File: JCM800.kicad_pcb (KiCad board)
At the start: 2 copper layers, 258.5 x 77.3 mm, 113 parts, among them U1 ECC83, U2 ECC83, U3 ECC83, U4 EL84, U5 EL84

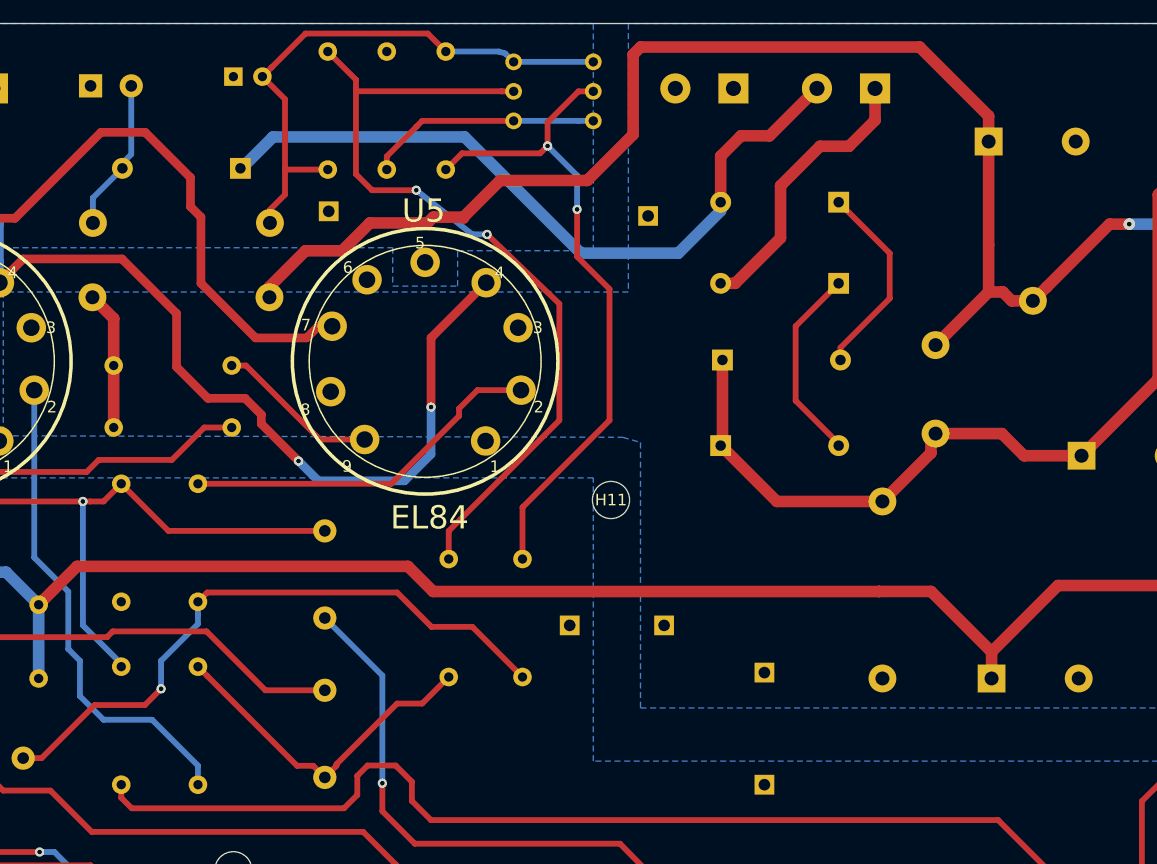
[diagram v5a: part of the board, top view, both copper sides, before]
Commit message: Fixed bias circuit
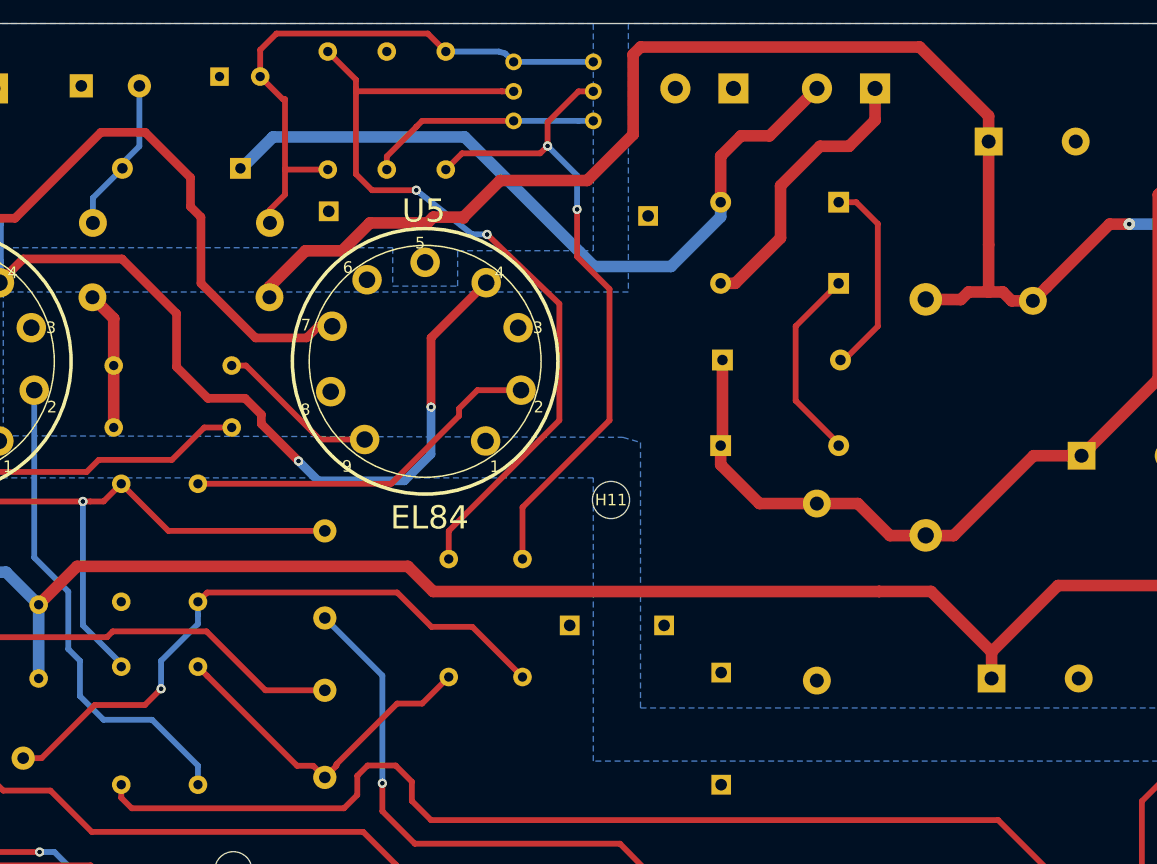
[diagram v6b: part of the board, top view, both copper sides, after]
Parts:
- C23: footprint Capacitor_THT:CP_Radial_D10.0mm_P3.50mm -> Capacitor_THT:CP_Radial_D10.0mm_P5.00mm
- C24: value 68uF/35V -> 100uF/35V; footprint Capacitor_THT:CP_Radial_D6.3mm_P2.50mm -> Capacitor_THT:CP_Radial_D8.0mm_P3.50mm
- R11: footprint Resistor_THT:R_Axial_DIN0922_L20.0mm_D9.0mm_P7.62mm_Vertical -> Resistor_THT:R_Axial_DIN0614_L14.3mm_D5.7mm_P20.32mm_Horizontal
- moved R8 5.65 mm to (240.2, 109.4)
- moved R11 4.03 mm to (249.6, 76.6)
- moved GND6 3.72 mm to (232.0, 108.7)
- moved GND7 3.72 mm to (232.0, 118.4)
- moved LOGO1 1.20 mm to (97.6, 108.9)
- moved C24 1.19 mm to (188.8, 57.4)
- moved C23 0.80 mm to (176.9, 58.2)
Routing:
- net /Tin2: track 63.6 -> 65.5 mm
- net Net-(BIAS_U4-Pad1): track 48.6 -> 50.3 mm
- net /A: track 75.4 -> 76.5 mm
- net /B: track 121.7 -> 120.9 mm
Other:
- rule pad_to_mask_clearance: 0.051 -> 0

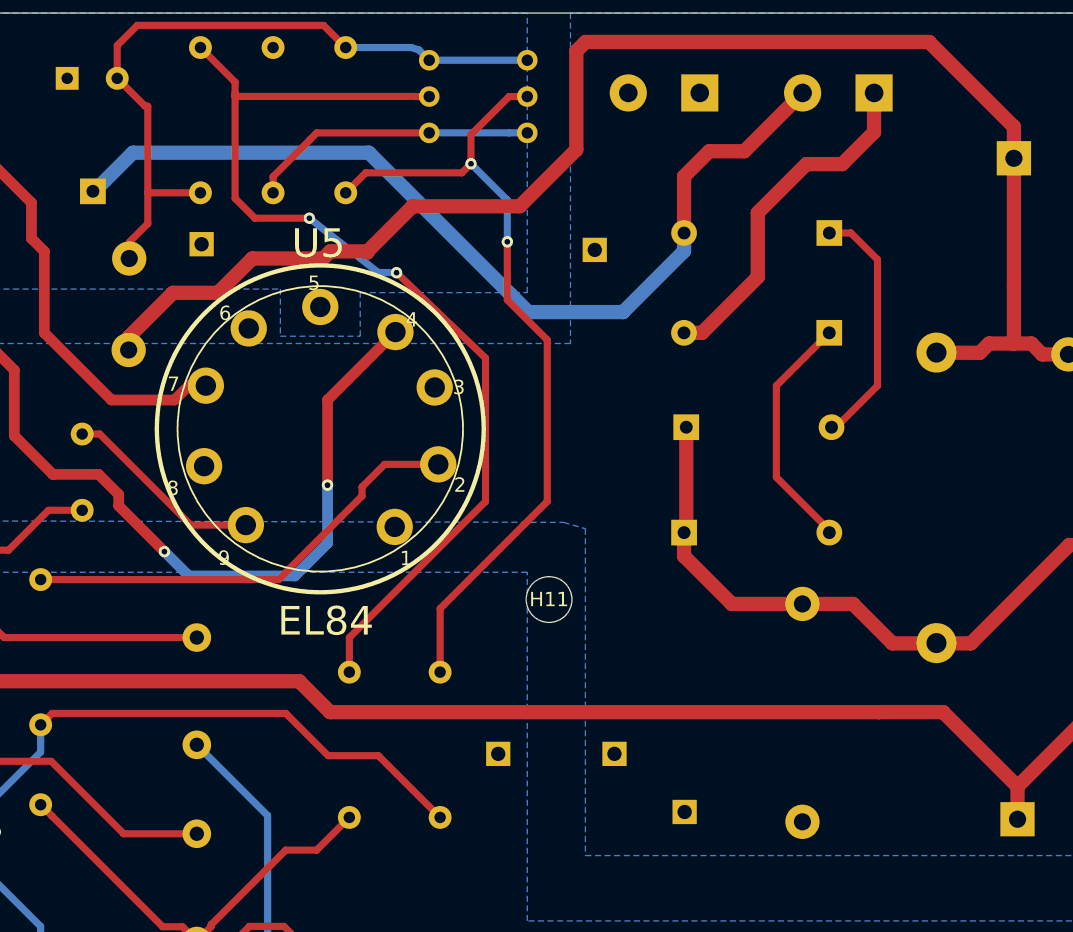
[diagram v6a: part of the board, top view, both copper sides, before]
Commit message: Fixed bias circuit
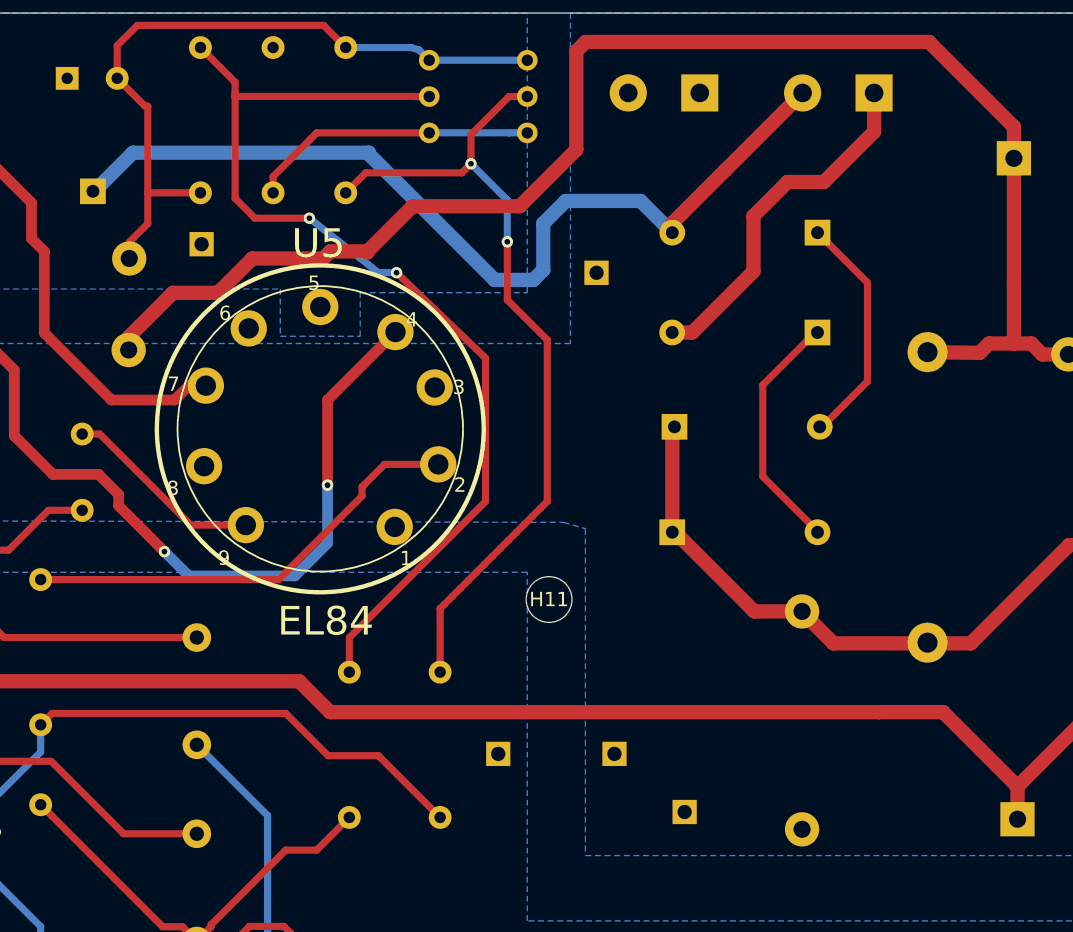
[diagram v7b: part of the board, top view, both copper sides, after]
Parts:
- moved GND1 1.60 mm to (225.8, 71.0)
- moved D2 0.83 mm to (241.3, 75.2)
- moved D4 0.83 mm to (241.3, 68.2)
- moved D1 0.83 mm to (231.1, 89.1)
- moved D3 0.83 mm to (231.3, 81.8)
- moved R11 0.63 mm to (249.0, 76.5)
- moved R8 0.53 mm to (240.2, 109.9)
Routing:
- net /Tin2: track 65.5 -> 64.0 mm
- net Net-(D3-Pad2): track 17.4 -> 16.5 mm
- net /B: track 120.9 -> 121.6 mm

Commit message: Cleanup
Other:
- net class Default removed
- net class EL84-CATHODE removed
- net class FIL removed
- net class GND removed
- net class HV_SIGNAL removed
- net class OUT removed
- net class PWR removed
